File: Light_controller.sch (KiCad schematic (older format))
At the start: 42 parts, among them U1 LM358, U10 PH2.0_horizontal, U11 PH2.0_horizontal, U12 PH2.0_horizontal, U13 PinSocket_1x4, U14 SMD2063, U2 PT8211-S, U3 STM8S003F3P, U4 SMD_2062, U5 tact_sw, U6 AMS1117-5.0, U7 EL357N-C, U8 EL357N-C, U9 PH2.0_horizontal

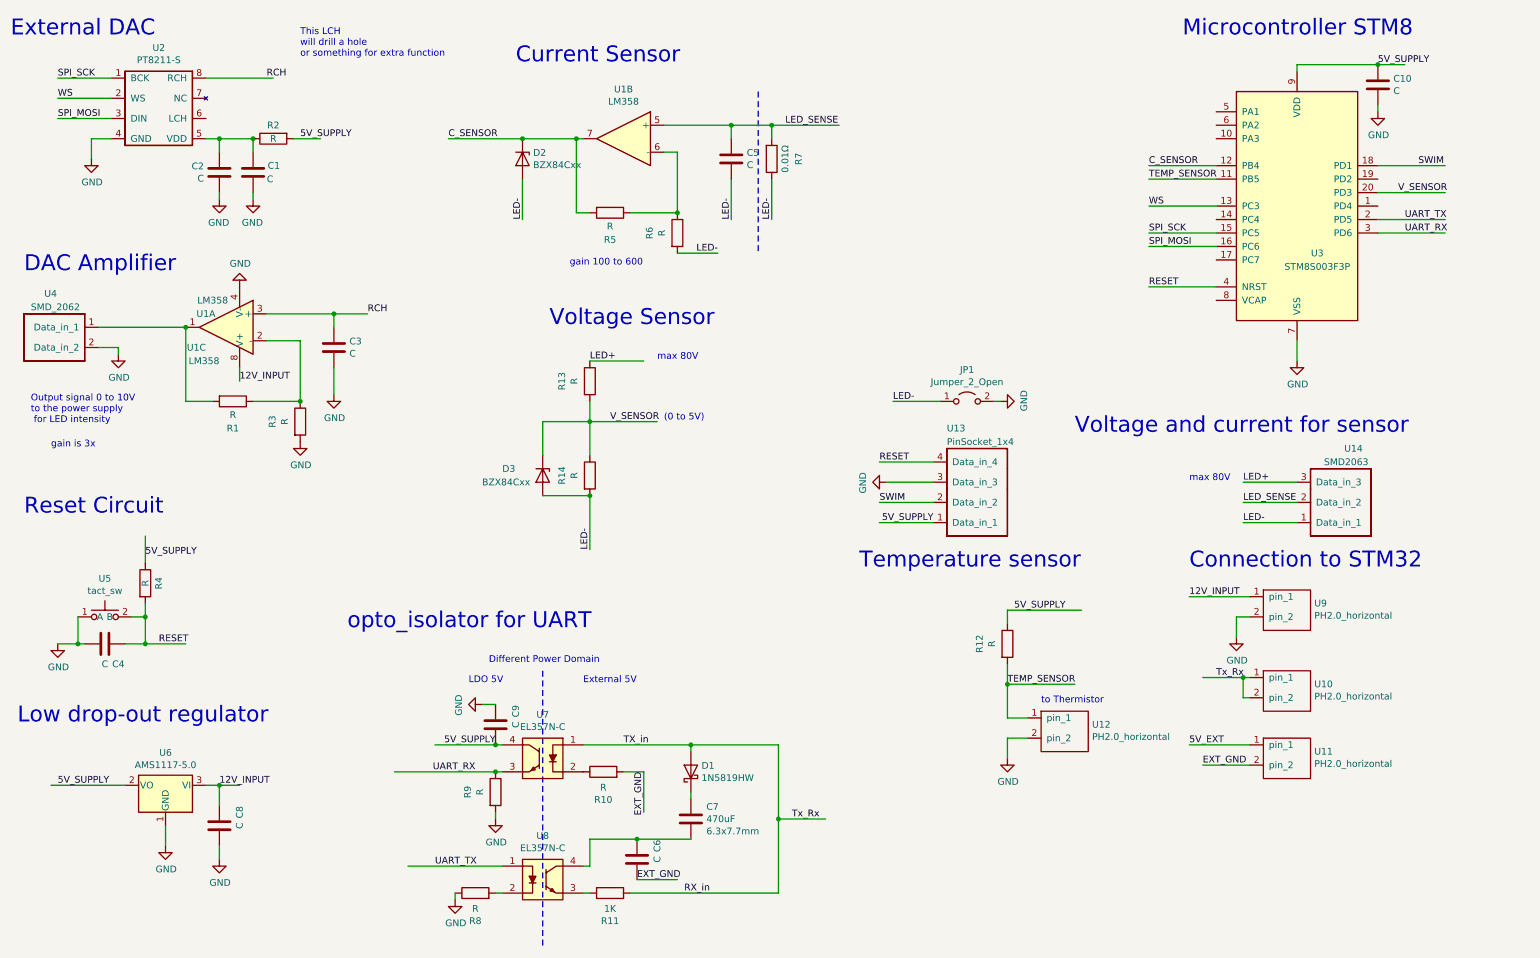
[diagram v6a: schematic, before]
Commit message: updated light controller pcb
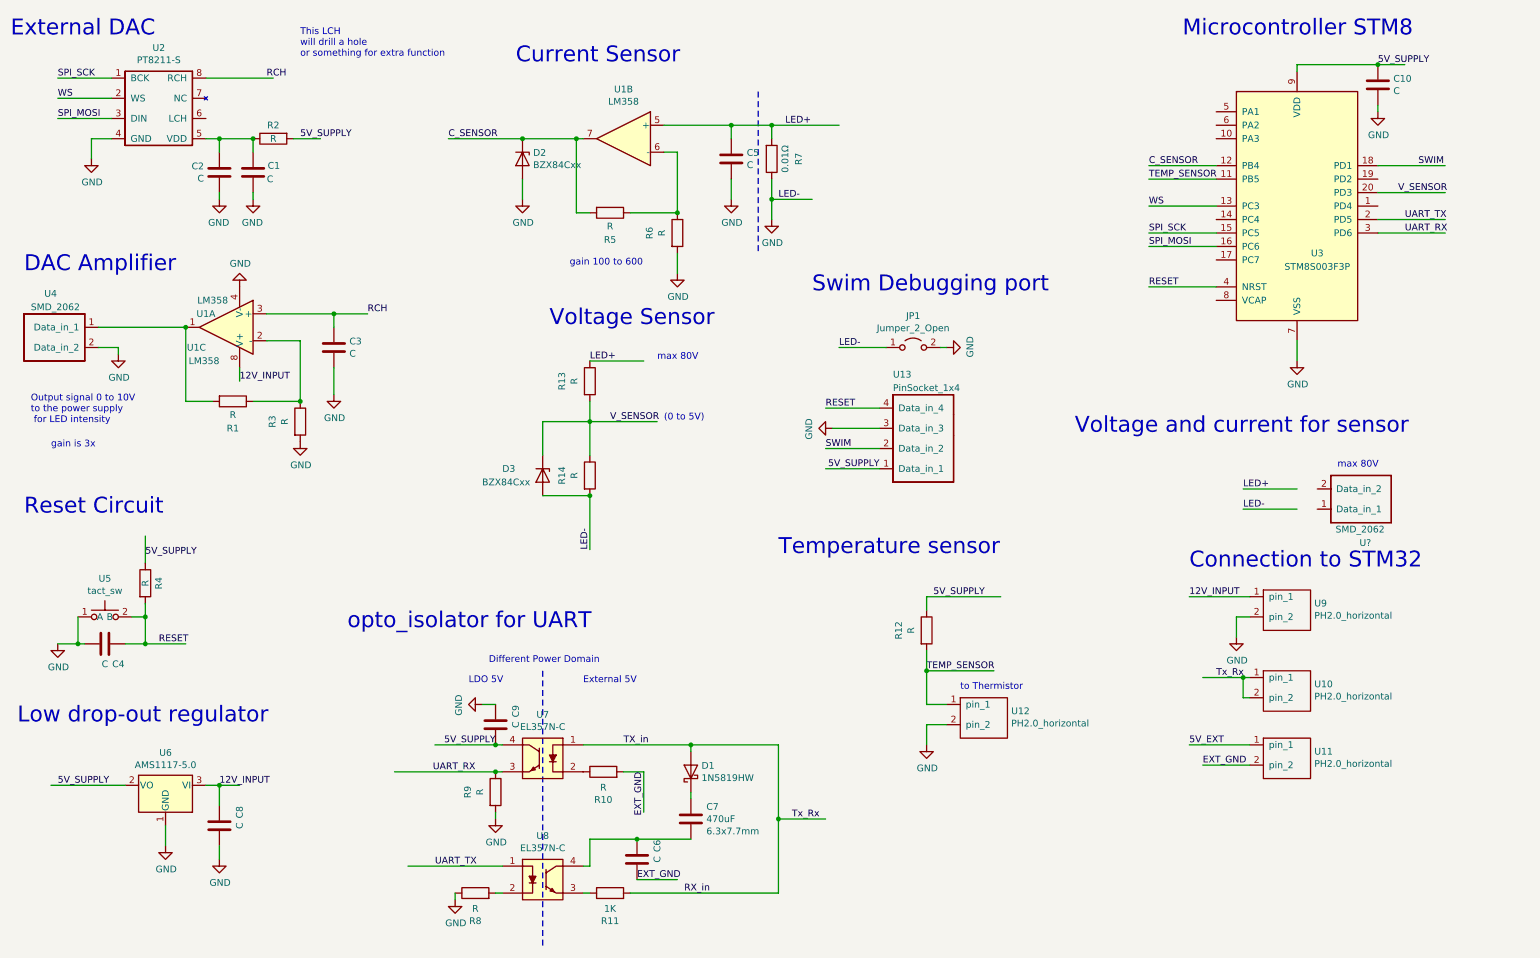
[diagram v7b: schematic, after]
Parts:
- removed U14: SMD2063, Custom_footprint_lib:SMD2063, symbol Custom_Library:SMD2063
- added U?: SMD_2062, Custom_footprint_lib:LEDSMD2062, symbol Custom_Library:SMD_2062
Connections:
- net labels removed: LED_SENSE
- wire segments 132 -> 133
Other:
- note added: "Swim Debugging port"
- moved on the sheet: JP1, R12, U12, U13
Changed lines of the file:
@@
 Text Label 2150 3200 0    50   ~ 0
 12V_INPUT
-Text Notes 6750 4600 0    118  ~ 0
+Text Notes 6150 4500 0    118  ~ 0
 Temperature sensor
 Wire Wire Line
-	8400 4900 7850 4900
-Text Label 7900 4900 0    50   ~ 0
+	7800 4800 7250 4800
+Text Label 7300 4800 0    50   ~ 0
 5V_SUPPLY
 $Comp
 L Device:R R12
 U 1 1 5E778979
-P 7850 5150
-F 0 "R12" V 7643 5150 50  0000 C CNN
-F 1 "R" V 7734 5150 50  0000 C CNN
-F 2 "Resistor_SMD:R_0603_1608Metric" V 7780 5150 50  0001 C CNN
-F 3 "~" H 7850 5150 50  0001 C CNN
-	1    7850 5150
-	1    0    0    -1
-$EndComp
-Wire Wire Line
-	7850 4900 7850 5000
+P 7250 5050
+F 0 "R12" V 7043 5050 50  0000 C CNN
+F 1 "R" V 7134 5050 50  0000 C CNN
+F 2 "Resistor_SMD:R_0603_1608Metric" V 7180 5050 50  0001 C CNN
+F 3 "~" H 7250 5050 50  0001 C CNN
+	1    7250 5050
+	1    0    0    -1
+$EndComp
+Wire Wire Line
+	7250 4800 7250 4900
 $Comp
 L power:GND #PWR01
 U 1 1 5E784F52
-P 7850 6000
-F 0 "#PWR01" H 7850 5750 50  0001 C CNN
-F 1 "GND" H 7855 5827 50  0000 C CNN
-F 2 "" H 7850 6000 50  0001 C CNN
-F 3 "" H 7850 6000 50  0001 C CNN
-	1    7850 6000
-	1    0    0    -1
-$EndComp
-Wire Wire Line
-	7850 5450 8350 5450
-Text Label 7850 5450 0    50   ~ 0
+P 7250 5900
+F 0 "#PWR01" H 7250 5650 50  0001 C CNN
+F 1 "GND" H 7255 5727 50  0000 C CNN
+F 2 "" H 7250 5900 50  0001 C CNN
+F 3 "" H 7250 5900 50  0001 C CNN
+	1    7250 5900
+	1    0    0    -1
+$EndComp
+Wire Wire Line
+	7250 5350 7750 5350
+Text Label 7250 5350 0    50   ~ 0
 TEMP_SENSOR
 $Comp
@@
 L Custom_Library:PH2.0_horizontal U12
 U 1 1 5E79BBBF
-P 8250 5600
-F 0 "U12" H 8478 5451 50  0000 L CNN
-F 1 "PH2.0_horizontal" H 8478 5360 50  0000 L CNN
-F 2 "Connector_JST:JST_PH_S2B-PH-SM4-TB_1x02-1MP_P2.00mm_Horizontal" H 8250 5600 50  0001 C CNN
-F 3 "" H 8250 5600 50  0001 C CNN
-	1    8250 5600
-	1    0    0    -1
-$EndComp
-Wire Wire Line
-	7850 5700 8000 5700
-Wire Wire Line
-	7850 5300 7850 5450
-Wire Wire Line
-	8000 5850 7850 5850
-Wire Wire Line
-	7850 5850 7850 6000
-Text Notes 8100 5600 0    50   ~ 0
+P 7650 5500
+F 0 "U12" H 7878 5351 50  0000 L CNN
+F 1 "PH2.0_horizontal" H 7878 5260 50  0000 L CNN
+F 2 "Connector_JST:JST_PH_S2B-PH-SM4-TB_1x02-1MP_P2.00mm_Horizontal" H 7650 5500 50  0001 C CNN
+F 3 "" H 7650 5500 50  0001 C CNN
+	1    7650 5500
+	1    0    0    -1
+$EndComp
+Wire Wire Line
+	7250 5600 7400 5600
+Wire Wire Line
+	7250 5200 7250 5350
+Wire Wire Line
+	7400 5750 7250 5750
+Wire Wire Line
+	7250 5750 7250 5900
+Text Notes 7500 5500 0    50   ~ 0
 to Thermistor
 $Comp
@@
 	-1   0    0    -1
 $EndComp
-Connection ~ 7850 5450
-Wire Wire Line
-	7850 5450 7850 5700
-$Comp
-L Custom_Library:SMD2063 U14
-U 1 1 5E8C06BF
-P 10350 4450
-F 0 "U14" H 10350 3700 50  0000 R CNN
-F 1 "SMD2063" H 10500 3800 50  0000 R CNN
-F 2 "Custom_footprint_lib:SMD2063" H 10350 4450 50  0001 C CNN
-F 3 "" H 10350 4450 50  0001 C CNN
-	1    10350 4450
-	-1   0    0    1
-$EndComp
-Text Label 9600 4250 0    50   ~ 0
+Connection ~ 7250 5350
+Wire Wire Line
+	7250 5350 7250 5600
+Text Label 9600 4150 0    50   ~ 0
 LED-
-Text Label 9600 3950 0    50   ~ 0
+Text Label 9600 4000 0    50   ~ 0
 LED+
-Text Label 9600 4100 0    50   ~ 0
-LED_SENSE
-Wire Wire Line
-	9600 4100 10000 4100
-Wire Wire Line
-	9600 3950 10000 3950
-Wire Wire Line
-	9600 4250 10000 4250
-Wire Wire Line
-	6100 1700 6100 2000
-Text Label 6100 2000 1    50   ~ 0
-LED-
+Wire Wire Line
+	9600 4000 10000 4000
+Wire Wire Line
+	9600 4150 10000 4150
 Text Label 6200 1300 0    50   ~ 0
-LED_SENSE
+LED+
 Text Notes 8350 3600 0    118  ~ 0
 Voltage and current for sensor
-$Comp
-L Device:R R13
-U 1 1 5E8FADD1
-P 4750 3200
-F 0 "R13" V 4543 3200 50  0000 C CNN
-F 1 "R" V 4634 3200 50  0000 C CNN
-F 2 "Resistor_SMD:R_0603_1608Metric" V 4680 3200 50  0001 C CNN
-F 3 "~" H 4750 3200 50  0001 C CNN
-	1    4750 3200
-	1    0    0    -1
-$EndComp
 Text Notes 4450 2800 0    118  ~ 0
 Voltage Sensor
@@
 Text Notes 5250 3050 0    50   ~ 0
 max 80V
-Text Notes 9200 3950 0    50   ~ 0
+Text Notes 10300 3850 0    50   ~ 0
 max 80V
 Text Notes 5300 3500 0    50   ~ 0
@@
 Wire Wire Line
 	4400 3500 4400 3750
-Wire Wire Line
-	5800 1700 5800 2000
-Text Label 5800 2000 1    50   ~ 0
-LED-
-Wire Wire Line
-	5400 2250 5700 2250
-Text Label 5700 2250 2    50   ~ 0
-LED-
 Text Label 3700 1400 0    50   ~ 0
 C_SENSOR
 Connection ~ 4650 1400
-Wire Wire Line
-	4250 1700 4250 2000
-Text Label 4250 2000 1    50   ~ 0
-LED-
 $Comp
 L Custom_Library:PinSocket_1x4 U13
 U 1 1 5E9927B0
-P 7600 4500
-F 0 "U13" H 7800 3550 50  0000 R CNN
-F 1 "PinSocket_1x4" H 7800 3650 50  0000 R CNN
-F 2 "Custom_footprint_lib:custom_pinsocket_1x04_p2.54" H 7600 4500 50  0001 C CNN
-F 3 "" H 7600 4500 50  0001 C CNN
-	1    7600 4500
+P 7200 4100
+F 0 "U13" H 7400 3150 50  0000 R CNN
+F 1 "PinSocket_1x4" H 7400 3250 50  0000 R CNN
+F 2 "Custom_footprint_lib:custom_pinsocket_1x04_p2.54" H 7200 4100 50  0001 C CNN
+F 3 "" H 7200 4100 50  0001 C CNN
+	1    7200 4100
 	-1   0    0    1
 $EndComp
 Wire Wire Line
-	7300 4100 6900 4100
-Wire Wire Line
-	7300 3800 6900 3800
-Text Label 6900 4100 0    50   ~ 0
+	6900 3700 6500 3700
+Wire Wire Line
+	6900 3400 6500 3400
+Text Label 6500 3700 0    50   ~ 0
 SWIM
-Text Label 6900 3800 0    50   ~ 0
+Text Label 6500 3400 0    50   ~ 0
 RESET
 $Comp
 L power:GND #PWR0103
 U 1 1 5E9FD433
-P 6950 3950
-F 0 "#PWR0103" H 6950 3700 50  0001 C CNN
-F 1 "GND" H 6955 3777 50  0000 C CNN
-F 2 "" H 6950 3950 50  0001 C CNN
-F 3 "" H 6950 3950 50  0001 C CNN
-	1    6950 3950
+P 6550 3550
+F 0 "#PWR0103" H 6550 3300 50  0001 C CNN
+F 1 "GND" H 6555 3377 50  0000 C CNN
+F 2 "" H 6550 3550 50  0001 C CNN
+F 3 "" H 6550 3550 50  0001 C CNN
+	1    6550 3550
 	0    1    1    0
 $EndComp
 Wire Wire Line
-	6950 3950 7300 3950
-Text Label 7300 4250 2    50   ~ 0
+	6550 3550 6900 3550
+Text Label 6900 3850 2    50   ~ 0
 5V_SUPPLY
 Wire Wire Line
-	6900 4250 7300 4250
+	6500 3850 6900 3850
 $Comp
 L Device:C C10
@@
 L power:GND #PWR0108
 U 1 1 5E7CE938
-P 7800 3350
-F 0 "#PWR0108" H 7800 3100 50  0001 C CNN
-F 1 "GND" H 7805 3177 50  0000 C CNN
-F 2 "" H 7800 3350 50  0001 C CNN
-F 3 "" H 7800 3350 50  0001 C CNN
-	1    7800 3350
+P 7400 2950
+F 0 "#PWR0108" H 7400 2700 50  0001 C CNN
+F 1 "GND" H 7405 2777 50  0000 C CNN
+F 2 "" H 7400 2950 50  0001 C CNN
+F 3 "" H 7400 2950 50  0001 C CNN
+	1    7400 2950
 	0    -1   -1   0
 $EndComp
 Wire Wire Line
-	7000 3350 7350 3350
-Text Label 7000 3350 0    50   ~ 0
+	6600 2950 6950 2950
+Text Label 6600 2950 0    50   ~ 0
 LED-
 $Comp
@@
 	4050 5900 4100 5900
 Wire Wire Line
-	7750 3350 7800 3350
+	7350 2950 7400 2950
 $Comp
 L Jumper:Jumper_2_Open JP1
 U 1 1 5E84B2E4
-P 7550 3350
-F 0 "JP1" H 7550 3585 50  0000 C CNN
-F 1 "Jumper_2_Open" H 7550 3494 50  0000 C CNN
-F 2 "Jumper:SolderJumper-2_P1.3mm_Open_TrianglePad1.0x1.5mm" H 7550 3350 50  0001 C CNN
-F 3 "~" H 7550 3350 50  0001 C CNN
-	1    7550 3350
-	1    0    0    -1
+P 7150 2950
+F 0 "JP1" H 7150 3185 50  0000 C CNN
+F 1 "Jumper_2_Open" H 7150 3094 50  0000 C CNN
+F 2 "Jumper:SolderJumper-2_P1.3mm_Open_TrianglePad1.0x1.5mm" H 7150 2950 50  0001 C CNN
+F 3 "~" H 7150 2950 50  0001 C CNN
+	1    7150 2950
+	1    0    0    -1
+$EndComp
+Wire Wire Line
+	6400 1850 6100 1850
+Text Label 6150 1850 0    50   ~ 0
+LED-
+Wire Wire Line
+	6100 1700 6100 1850
+$Comp
+L power:GND #PWR?
+U 1 1 5FB5CA1C
+P 6100 2000
+F 0 "#PWR?" H 6100 1750 50  0001 C CNN
+F 1 "GND" H 6105 1827 50  0000 C CNN
+F 2 "" H 6100 2000 50  0001 C CNN
+F 3 "" H 6100 2000 50  0001 C CNN
+	1    6100 2000
+	1    0    0    -1
+$EndComp
+Wire Wire Line
+	6100 2000 6100 1850
+Connection ~ 6100 1850
+$Comp
+L power:GND #PWR?
+U 1 1 5FB7DBB9
+P 5800 1850
+F 0 "#PWR?" H 5800 1600 50  0001 C CNN
+F 1 "GND" H 5805 1677 50  0000 C CNN
+F 2 "" H 5800 1850 50  0001 C CNN
+F 3 "" H 5800 1850 50  0001 C CNN
+	1    5800 1850
+	1    0    0    -1
+$EndComp
+Wire Wire Line
+	5800 1850 5800 1700
+$Comp
+L power:GND #PWR?
+U 1 1 5FB87DEB
+P 5400 2400
+F 0 "#PWR?" H 5400 2150 50  0001 C CNN
+F 1 "GND" H 5405 2227 50  0000 C CNN
+F 2 "" H 5400 2400 50  0001 C CNN
+F 3 "" H 5400 2400 50  0001 C CNN
+	1    5400 2400
+	1    0    0    -1
+$EndComp
+Wire Wire Line
+	5400 2400 5400 2250
+$Comp
+L power:GND #PWR?
+U 1 1 5FB918D1
+P 4250 1850
+F 0 "#PWR?" H 4250 1600 50  0001 C CNN
+F 1 "GND" H 4255 1677 50  0000 C CNN
+F 2 "" H 4250 1850 50  0001 C CNN
+F 3 "" H 4250 1850 50  0001 C CNN
+	1    4250 1850
+	1    0    0    -1
+$EndComp
+Wire Wire Line
+	4250 1850 4250 1700
+$Comp
+L Device:R R13
+U 1 1 5E8FADD1
+P 4750 3200
+F 0 "R13" V 4543 3200 50  0000 C CNN
+F 1 "R" V 4634 3200 50  0000 C CNN
+F 2 "Resistor_SMD:R_0603_1608Metric" V 4680 3200 50  0001 C CNN
+F 3 "~" H 4750 3200 50  0001 C CNN
+	1    4750 3200
+	1    0    0    -1
+$EndComp
+Text Notes 6400 2550 0    118  ~ 0
+Swim Debugging port
+$Comp
+L Custom_Library:SMD_2062 U?
+U 1 1 5FB97485
+P 10400 4300
+F 0 "U?" H 10250 4400 50  0000 L CNN
+F 1 "SMD_2062" H 10150 4300 50  0000 L CNN
+F 2 "Custom_footprint_lib:LEDSMD2062" H 10400 4300 50  0001 C CNN
+F 3 "" H 10400 4300 50  0001 C CNN
+	1    10400 4300
+	-1   0    0    1
 $EndComp
 $EndSCHEMATC

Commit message: added comment for sensor resistor resistance
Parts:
- removed C1, C2, C3: C, Capacitor_SMD:C_0805_2012Metric, symbol Device:C
- removed R1, R2, R3: R, Resistor_SMD:R_0603_1608Metric, symbol Device:R
- removed unit 2 of U1
- removed U2: PT8211-S, Package_SO:SOP-8_3.9x4.9mm_P1.27mm, symbol Custom_Library:PT8211
- removed U?: SMD_2062, Custom_footprint_lib:LEDSMD2062, symbol Custom_Library:SMD_2062
- added C?: C, Capacitor_SMD:C_0805_2012Metric, symbol Device:C
- added D? (x2): BZX84Cxx, Diode_SMD:D_SOT-23_ANK, symbol Diode:BZX84Cxx
- added D? (x3): D, symbol Device:D
- added Q? (x2): Q_NMOS_GSD, Package_TO_SOT_SMD:SOT-23, symbol Device:Q_NMOS_GSD
- added R?: R, Resistor_SMD:R_0603_1608Metric, symbol Device:R
- added U?: SMD2063, Custom_footprint_lib:SMD2063, symbol Custom_Library:SMD2063
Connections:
- net labels added: LED_SENSE, PWM_OUT
- net labels removed: RCH, SPI_MOSI, SPI_SCK, WS
- wire segments 133 -> 132
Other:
- note added: "0.0625 X resistor\n"
- note added: "18.3K"
- note added: "X\n"
- note added: "around 10V\n"
- note added: "gain 160\n"
- note removed: "DAC Amplifier"
- note removed: "External DAC"
- note removed: "Output signal 0 to 10V\nto the power supply\n for LED intensity\n\n"
- note removed: "This LCH \nwill drill a hole \nor something for extra function\n"
- note removed: "gain 100 to 600"
- note removed: "gain is 3x\n"
- moved on the sheet: C5, D2, JP1, R12, R5, R6, R7, U12, U13, U1A, U1C, U4
